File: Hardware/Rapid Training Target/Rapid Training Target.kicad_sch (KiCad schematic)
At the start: 15 parts, among them Q1 2N7002, Q2 2N7002, Q3 2N7002

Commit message: added code and remote
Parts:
- removed U1: ~, Personal:ESP32-C3-DevKit, symbol personal2:ESP32-C3_DevKit_Rev_A
- added C1, C2: 1u, Capacitor_SMD:C_0603_1608Metric, symbol Device:C
- added R1, R2: 5k1, Resistor_SMD:R_0603_1608Metric, symbol Device:R
- added U2: MIC5504-3.3YM5, Package_TO_SOT_SMD:SOT-23-5, symbol Regulator_Linear:MIC5504-3.3YM5
- added U3: ESP32-C3-MINI-1-N4, Personal:ESP32-­C3-­MINI­-1, symbol personal2:ESP32-­C3-­MINI­-1
- added USB-C1: USB-C-16P-F(A40-00119-A52-12), Personal:USB2.0_TYPE-C(A40-00119-A52-12), symbol personal2:USB2.0_TYPE-C(A40-00119-A52-12)
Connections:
- net +3V3: now also C1.1, U2.5 (VOUT), U3.3 (3V3), U3.8 (EN)
- net +5V: now also C2.1, U2.1 (VIN), U2.3 (EN), USB-C1.A4 (VBUS), USB-C1.A9 (VBUS), USB-C1.B4 (VBUS), USB-C1.B9 (VBUS)
- net Blue: now also U3.20 (IO6/GPIO6/FSPICLK/MTCK)
- net GND: now also C1.2, C2.2, R1.2, R2.2, U2.2 (GND), U3.1 (GND), U3.11 (GND), U3.14 (GND), U3.2 (GND), U3.36 (GND), U3.37 (GND), U3.38 (GND), U3.39 (GND), U3.40 (GND), U3.41 (GND), U3.42 (GND), U3.43 (GND), U3.44 (GND), U3.45 (GND), U3.46 (GND), U3.47 (GND), U3.48 (GND), U3.49 (GND), U3.50 (GND), U3.51 (GND), U3.52 (GND), U3.53 (GND), USB-C1.0 (SHELL), USB-C1.A1 (GND), USB-C1.A12 (GND), USB-C1.B1 (GND), USB-C1.B12 (GND)
- net Green: now also U3.19 (IO5/GPIO5/ADC2_CH0/FSPIWP/MTDI)
- net Red: now also U3.18 (IO4/GPIO4/ADC1_CH4/FSPIHD/MTMS)
- new net: R2.1, USB-C1.A5 (CC1)
- new net: R1.1, USB-C1.B5 (CC2)
- new net USB_D+: U3.27 (IO19/GPIO19/USB_D+), USB-C1.A6 (DP1), USB-C1.B6 (DP2)
- new net USB_D-: U3.26 (IO18/GPIO18/USB_D-), USB-C1.A7 (DN1), USB-C1.B7 (DN2)
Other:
- moved on the sheet: H1, H2, H3

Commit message: added logo
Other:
- note added: "Blue: 2.2V 1mA 25mcd 2.2k"
- note added: "Green: 2.3V 1mA 130mcd 120k"
- note added: "Red: 3.2V 1mA 45mcd 5.76k"
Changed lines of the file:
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@@
     (stroke (width 0) (type default))
+  )
+  (text "Green:\n2.3V\n1mA\n130mcd\n120k\n" (at 111.76 35.56 0)
+    (effects (font (size 1.27 1.27)) (justify left bottom))
+  )
+  (text "Blue:\n2.2V\n1mA\n25mcd\n2.2k\n" (at 119.38 35.56 0)
+    (effects (font (size 1.27 1.27)) (justify left bottom))
+  )
+  (text "Red:\n3.2V\n1mA\n45mcd\n5.76k\n" (at 104.14 35.56 0)
+    (effects (font (size 1.27 1.27)) (justify left bottom))
   )
   (global_label "Red" (shape input) (at 214.63 77.47 0) (fields_autoplaced)

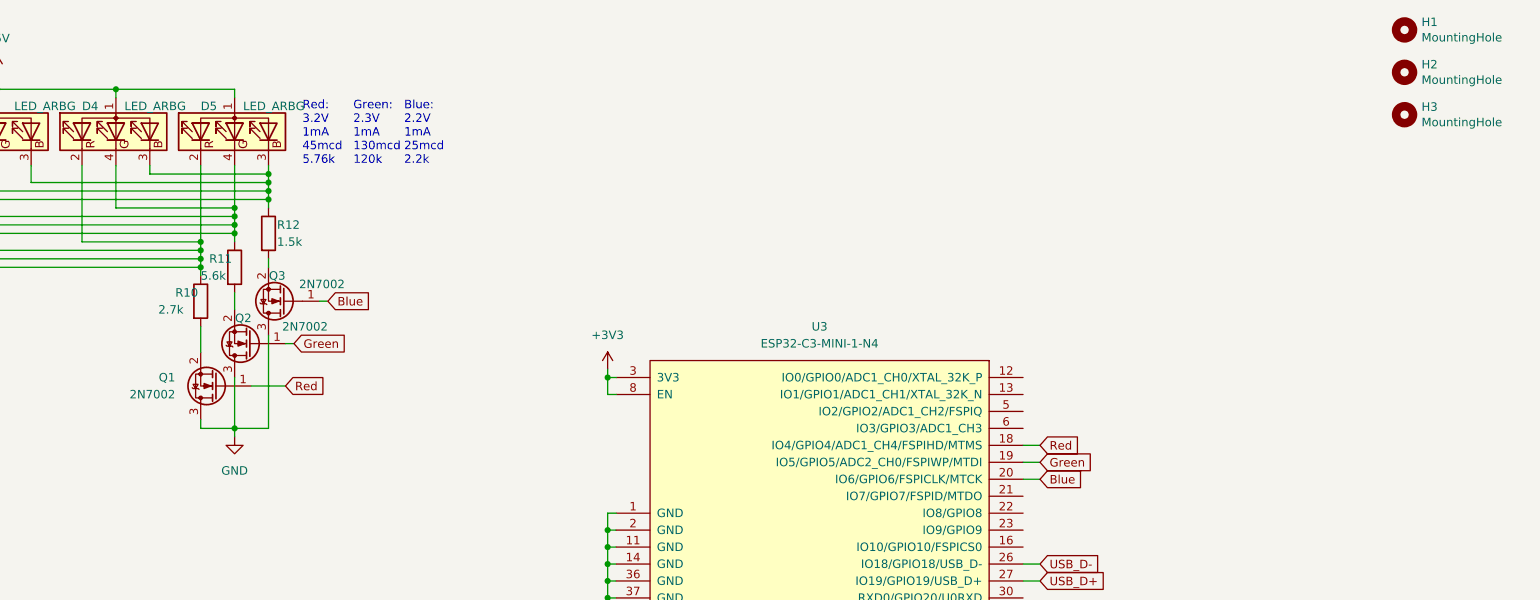
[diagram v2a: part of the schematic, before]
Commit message: rounded off edges and created a step
removed the use of mosfets for driving leds as found to be obsolete. Rounded corners, added a size indicator. changed the
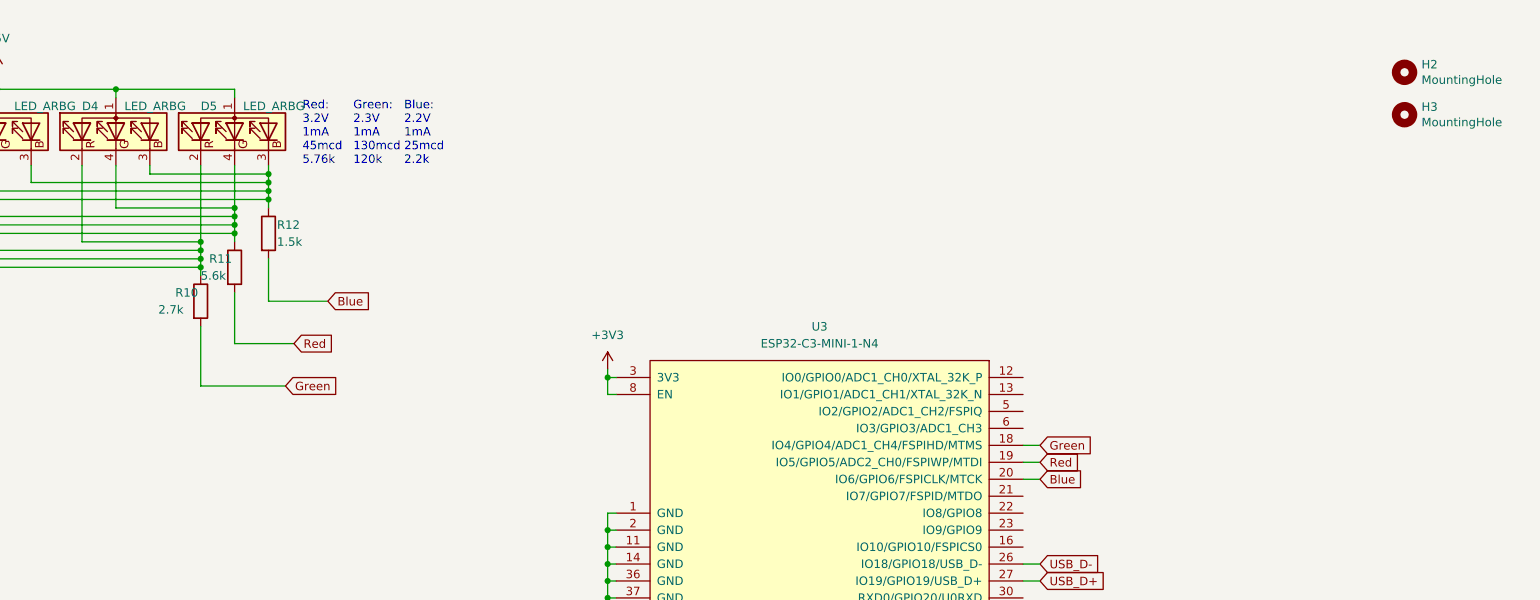
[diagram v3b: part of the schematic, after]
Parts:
- removed H1: MountingHole, MountingHole:MountingHole_3.2mm_M3_DIN965_Pad, symbol Mechanical:MountingHole
- removed Q1, Q2, Q3: 2N7002, Package_TO_SOT_SMD:SOT-23, symbol Transistor_FET:2N7002
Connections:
- net Blue: now also R12.2
- net Green: now also R10.2, U3.18 (IO4/GPIO4/ADC1_CH4/FSPIHD/MTMS); no longer U3.19 (IO5/GPIO5/ADC2_CH0/FSPIWP/MTDI)
- net Red: now also R11.2, U3.19 (IO5/GPIO5/ADC2_CH0/FSPIWP/MTDI); no longer U3.18 (IO4/GPIO4/ADC1_CH4/FSPIHD/MTMS)

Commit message: added initial cad
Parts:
- renumbered R11 to R1, R12 to R2, R10 to R3, R2 to R4, R1 to R5, U2 to U1, U3 to U2
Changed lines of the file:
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@@
   (symbol (lib_id "Device:R") (at 38.1 166.37 0) (mirror y) (unit 1)
     (in_bom yes) (on_board yes) (dnp no) (fields_autoplaced)
-    (property "Reference" "R2" (at 40.64 165.1 0)
+    (property "Reference" "R4" (at 40.64 165.1 0)
       (effects (font (size 1.27 1.27)) (justify right))
     )
@@
       (project "Rapid Training Target"
         (path "/9fedd953-8356-4168-99e6-03d50e1e6951"
-          (reference "R2") (unit 1)
+          (reference "R4") (unit 1)
         )
       )
@@
   (symbol (lib_id "Device:R") (at 88.9 55.88 0) (unit 1)
     (in_bom yes) (on_board yes) (dnp no)
-    (property "Reference" "R10" (at 85.09 54.61 0)
+    (property "Reference" "R3" (at 85.09 54.61 0)
       (effects (font (size 1.27 1.27)) (justify left))
     )
@@
       (project "Rapid Training Target"
         (path "/9fedd953-8356-4168-99e6-03d50e1e6951"
-          (reference "R10") (unit 1)
+          (reference "R3") (unit 1)
         )
       )
@@
   (symbol (lib_id "Device:R") (at 99.06 45.72 0) (unit 1)
     (in_bom yes) (on_board yes) (dnp no)
-    (property "Reference" "R12" (at 100.33 44.45 0)
+    (property "Reference" "R2" (at 100.33 44.45 0)
       (effects (font (size 1.27 1.27)) (justify left))
     )
@@
       (project "Rapid Training Target"
         (path "/9fedd953-8356-4168-99e6-03d50e1e6951"
-          (reference "R12") (unit 1)
+          (reference "R2") (unit 1)
         )
       )
@@
   (symbol (lib_id "personal2:ESP32-­C3-­MINI­-1") (at 207.01 64.77 0) (mirror y) (unit 1)
     (in_bom yes) (on_board yes) (dnp no)
-    (property "Reference" "U3" (at 181.61 59.69 0)
+    (property "Reference" "U2" (at 181.61 59.69 0)
       (effects (font (size 1.27 1.27)))
     )
@@
       (project "Rapid Training Target"
         (path "/9fedd953-8356-4168-99e6-03d50e1e6951"
-          (reference "U3") (unit 1)
+          (reference "U2") (unit 1)
         )
       )
@@
   (symbol (lib_id "Device:R") (at 35.56 166.37 0) (unit 1)
     (in_bom yes) (on_board yes) (dnp no)
-    (property "Reference" "R1" (at 33.02 165.1 0)
+    (property "Reference" "R5" (at 33.02 165.1 0)
       (effects (font (size 1.27 1.27)) (justify right))
     )
@@
       (project "Rapid Training Target"
         (path "/9fedd953-8356-4168-99e6-03d50e1e6951"
-          (reference "R1") (unit 1)
+          (reference "R5") (unit 1)
         )
       )
@@
   (symbol (lib_id "Regulator_Linear:MIC5504-3.3YM5") (at 34.29 104.14 0) (unit 1)
     (in_bom yes) (on_board yes) (dnp no) (fields_autoplaced)
-    (property "Reference" "U2" (at 34.29 93.98 0)
+    (property "Reference" "U1" (at 34.29 93.98 0)
       (effects (font (size 1.27 1.27)))
     )
@@
       (project "Rapid Training Target"
         (path "/9fedd953-8356-4168-99e6-03d50e1e6951"
-          (reference "U2") (unit 1)
+          (reference "U1") (unit 1)
         )
       )
@@
   (symbol (lib_id "Device:R") (at 93.98 50.8 0) (unit 1)
     (in_bom yes) (on_board yes) (dnp no)
-    (property "Reference" "R11" (at 90.17 49.53 0)
+    (property "Reference" "R1" (at 90.17 49.53 0)
       (effects (font (size 1.27 1.27)) (justify left))
     )
@@
       (project "Rapid Training Target"
         (path "/9fedd953-8356-4168-99e6-03d50e1e6951"
-          (reference "R11") (unit 1)
-        )
-      )
+          (reference "R1") (unit 1)
+        )
+      )

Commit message: changes to 3.3v
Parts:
- renumbered C2 to C1, C1 to C2, H2 to H1, H3 to H2, R4 to R1, R1 to R2, R2 to R3, R3 to R4
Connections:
- net +3V3: now also D1.1 (A), D2.1 (A), D3.1 (A), D4.1 (A), D5.1 (A)
- net +5V: no longer D1.1 (A), D2.1 (A), D3.1 (A), D4.1 (A), D5.1 (A)
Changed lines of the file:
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@@
-    )
-  )
-  (symbol (lib_id "power:+5V") (at 58.42 21.59 0) (unit 1)
-    (in_bom yes) (on_board yes) (dnp no) (fields_autoplaced)
-    (property "Reference" "#PWR03" (at 58.42 25.4 0)
-      (effects (font (size 1.27 1.27)) hide)
-    )
-    (property "Value" "+5V" (at 58.42 16.51 0)
-      (effects (font (size 1.27 1.27)))
-    )
-    (property "Footprint" "" (at 58.42 21.59 0)
-      (effects (font (size 1.27 1.27)) hide)
-    )
-    (property "Datasheet" "" (at 58.42 21.59 0)
-      (effects (font (size 1.27 1.27)) hide)
-    )
-    (pin "1")
-    (instances
-      (project "Rapid Training Target"
-        (path "/9fedd953-8356-4168-99e6-03d50e1e6951"
-          (reference "#PWR03") (unit 1)
-        )
-      )
-      (project "Training Aid-B"
-        (path "/e219089c-061e-4d60-9bdd-f96cb714b740"
-          (reference "#PWR0102") (unit 1)
-        )
-      )
     )
   )
@@
   (symbol (lib_id "Device:R") (at 38.1 166.37 0) (mirror y) (unit 1)
     (in_bom yes) (on_board yes) (dnp no) (fields_autoplaced)
-    (property "Reference" "R4" (at 40.64 165.1 0)
+    (property "Reference" "R1" (at 40.64 165.1 0)
       (effects (font (size 1.27 1.27)) (justify right))
     )
@@
       (project "Rapid Training Target"
         (path "/9fedd953-8356-4168-99e6-03d50e1e6951"
-          (reference "R4") (unit 1)
+          (reference "R1") (unit 1)
         )
       )
@@
   (symbol (lib_id "Device:C") (at 45.72 106.68 0) (unit 1)
     (in_bom yes) (on_board yes) (dnp no) (fields_autoplaced)
-    (property "Reference" "C1" (at 49.53 105.41 0)
+    (property "Reference" "C2" (at 49.53 105.41 0)
       (effects (font (size 1.27 1.27)) (justify left))
     )
@@
       (project "Rapid Training Target"
         (path "/9fedd953-8356-4168-99e6-03d50e1e6951"
-          (reference "C1") (unit 1)
+          (reference "C2") (unit 1)
         )
       )
@@
   (symbol (lib_id "Mechanical:MountingHole") (at 269.24 21.59 0) (unit 1)
     (in_bom yes) (on_board yes) (dnp no)
-    (property "Reference" "H2" (at 271.78 20.4216 0)
+    (property "Reference" "H1" (at 271.78 20.4216 0)
       (effects (font (size 1.27 1.27)) (justify left))
     )
@@
       (project "Rapid Training Target"
         (path "/9fedd953-8356-4168-99e6-03d50e1e6951"
+          (reference "H1") (unit 1)
+        )
+      )
+      (project "Training Aid-B"
+        (path "/e219089c-061e-4d60-9bdd-f96cb714b740"
           (reference "H2") (unit 1)
         )
       )
-      (project "Training Aid-B"
-        (path "/e219089c-061e-4d60-9bdd-f96cb714b740"
+    )
+  )
+  (symbol (lib_id "Mechanical:MountingHole") (at 269.24 27.94 0) (unit 1)
+    (in_bom yes) (on_board yes) (dnp no)
+    (property "Reference" "H2" (at 271.78 26.7716 0)
+      (effects (font (size 1.27 1.27)) (justify left))
+    )
+    (property "Value" "MountingHole" (at 271.78 29.083 0)
+      (effects (font (size 1.27 1.27)) (justify left))
+    )
+    (property "Footprint" "MountingHole:MountingHole_3.2mm_M3_DIN965_Pad" (at 269.24 27.94 0)
+      (effects (font (size 1.27 1.27)) hide)
+    )
+    (property "Datasheet" "~" (at 269.24 27.94 0)
+      (effects (font (size 1.27 1.27)) hide)
+    )
+    (instances
+      (project "Rapid Training Target"
+        (path "/9fedd953-8356-4168-99e6-03d50e1e6951"
           (reference "H2") (unit 1)
-        )
-      )
-    )
-  )
-  (symbol (lib_id "Mechanical:MountingHole") (at 269.24 27.94 0) (unit 1)
-    (in_bom yes) (on_board yes) (dnp no)
-    (property "Reference" "H3" (at 271.78 26.7716 0)
-      (effects (font (size 1.27 1.27)) (justify left))
-    )
-    (property "Value" "MountingHole" (at 271.78 29.083 0)
-      (effects (font (size 1.27 1.27)) (justify left))
-    )
-    (property "Footprint" "MountingHole:MountingHole_3.2mm_M3_DIN965_Pad" (at 269.24 27.94 0)
-      (effects (font (size 1.27 1.27)) hide)
-    )
-    (property "Datasheet" "~" (at 269.24 27.94 0)
-      (effects (font (size 1.27 1.27)) hide)
-    )
-    (instances
-      (project "Rapid Training Target"
-        (path "/9fedd953-8356-4168-99e6-03d50e1e6951"
-          (reference "H3") (unit 1)
         )
       )
@@
     )
   )
+  (symbol (lib_id "power:+3V3") (at 58.42 21.59 0) (unit 1)
+    (in_bom yes) (on_board yes) (dnp no) (fields_autoplaced)
+    (property "Reference" "#PWR02" (at 58.42 25.4 0)
+      (effects (font (size 1.27 1.27)) hide)
+    )
+    (property "Value" "+3V3" (at 58.42 16.51 0)
+      (effects (font (size 1.27 1.27)))
+    )
+    (property "Footprint" "" (at 58.42 21.59 0)
+      (effects (font (size 1.27 1.27)) hide)
+    )
+    (property "Datasheet" "" (at 58.42 21.59 0)
+      (effects (font (size 1.27 1.27)) hide)
+    )
+    (pin "1")
+    (instances
+      (project "Rapid Training Target"
+        (path "/9fedd953-8356-4168-99e6-03d50e1e6951"
+          (reference "#PWR02") (unit 1)
+        )
+      )
+    )
+  )
   (symbol (lib_name "+5V_2") (lib_id "power:+5V") (at 30.48 129.54 0) (unit 1)
     (in_bom yes) (on_board yes) (dnp no) (fields_autoplaced)
@@
   (symbol (lib_id "Device:R") (at 88.9 55.88 0) (unit 1)
     (in_bom yes) (on_board yes) (dnp no)
-    (property "Reference" "R3" (at 85.09 54.61 0)
+    (property "Reference" "R4" (at 85.09 54.61 0)
       (effects (font (size 1.27 1.27)) (justify left))
     )
@@
       (project "Rapid Training Target"
         (path "/9fedd953-8356-4168-99e6-03d50e1e6951"
-          (reference "R3") (unit 1)
+          (reference "R4") (unit 1)
         )
       )
@@
   (symbol (lib_id "Device:R") (at 99.06 45.72 0) (unit 1)
     (in_bom yes) (on_board yes) (dnp no)
-    (property "Reference" "R2" (at 100.33 44.45 0)
+    (property "Reference" "R3" (at 100.33 44.45 0)
       (effects (font (size 1.27 1.27)) (justify left))
     )
@@
       (project "Rapid Training Target"
         (path "/9fedd953-8356-4168-99e6-03d50e1e6951"
-          (reference "R2") (unit 1)
+          (reference "R3") (unit 1)
         )
       )
@@
   (symbol (lib_id "Device:C") (at 21.59 106.68 0) (mirror y) (unit 1)
     (in_bom yes) (on_board yes) (dnp no)
-    (property "Reference" "C2" (at 17.78 105.41 0)
+    (property "Reference" "C1" (at 17.78 105.41 0)
       (effects (font (size 1.27 1.27)) (justify left))
     )
@@
       (project "Rapid Training Target"
         (path "/9fedd953-8356-4168-99e6-03d50e1e6951"
-          (reference "C2") (unit 1)
+          (reference "C1") (unit 1)
         )
       )
@@
   (symbol (lib_id "Device:R") (at 93.98 50.8 0) (unit 1)
     (in_bom yes) (on_board yes) (dnp no)
-    (property "Reference" "R1" (at 90.17 49.53 0)
+    (property "Reference" "R2" (at 90.17 49.53 0)
       (effects (font (size 1.27 1.27)) (justify left))
     )
@@
       (project "Rapid Training Target"
         (path "/9fedd953-8356-4168-99e6-03d50e1e6951"
-          (reference "R1") (unit 1)
-        )
-      )
+          (reference "R2") (unit 1)
+        )
+      )

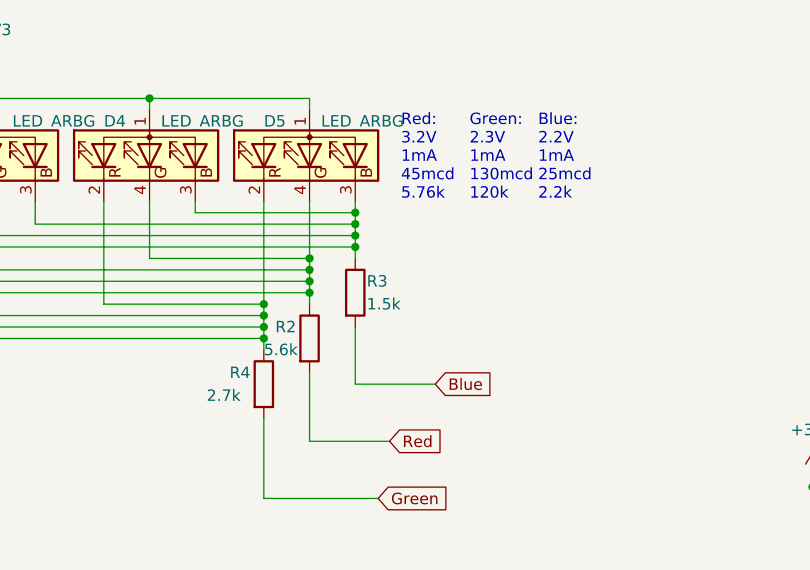
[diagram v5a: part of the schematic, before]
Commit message: changed to 0603 capacitors
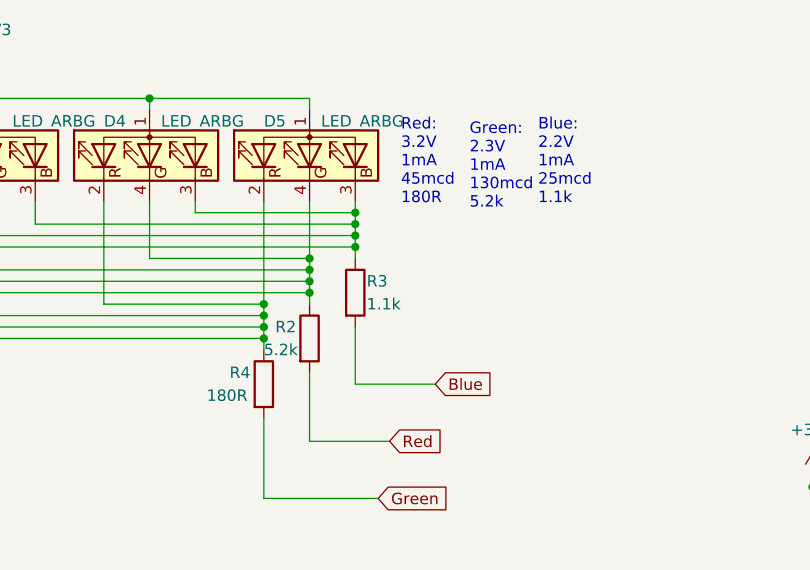
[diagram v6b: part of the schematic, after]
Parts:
- R2: value 5.6k -> 5.2k
- R3: value 1.5k -> 1.1k
- R4: value 2.7k -> 180R
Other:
- note added: "Blue: 2.2V 1mA 25mcd 1.1k"
- note added: "Green: 2.3V 1mA 130mcd 5.2k"
- note added: "Red: 3.2V 1mA 45mcd 180R"
- note removed: "Blue: 2.2V 1mA 25mcd 2.2k"
- note removed: "Green: 2.3V 1mA 130mcd 120k"
- note removed: "Red: 3.2V 1mA 45mcd 5.76k"
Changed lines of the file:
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@@
     (stroke (width 0) (type default))
   )
-  (text "Green:\n2.3V\n1mA\n130mcd\n120k\n" (at 111.76 35.56 0)
+  (text "Green:\n2.3V\n1mA\n130mcd\n5.2k\n\n\n" (at 111.76 40.64 0)
     (effects (font (size 1.27 1.27)) (justify left bottom))
   )
-  (text "Blue:\n2.2V\n1mA\n25mcd\n2.2k\n" (at 119.38 35.56 0)
+  (text "Blue:\n2.2V\n1mA\n25mcd\n1.1k\n\n" (at 119.38 38.1 0)
     (effects (font (size 1.27 1.27)) (justify left bottom))
   )
-  (text "Red:\n3.2V\n1mA\n45mcd\n5.76k\n" (at 104.14 35.56 0)
+  (text "Red:\n3.2V\n1mA\n45mcd\n180R\n\n" (at 104.14 38.1 0)
     (effects (font (size 1.27 1.27)) (justify left bottom))
   )
@@
       (effects (font (size 1.27 1.27)) (justify left))
     )
-    (property "Value" "2.7k" (at 82.55 57.15 0)
+    (property "Value" "180R" (at 82.55 57.15 0)
       (effects (font (size 1.27 1.27)) (justify left))
     )
@@
       (effects (font (size 1.27 1.27)) (justify left))
     )
-    (property "Value" "1.5k" (at 100.33 46.99 0)
+    (property "Value" "1.1k" (at 100.33 46.99 0)
       (effects (font (size 1.27 1.27)) (justify left))
     )
@@
       (effects (font (size 1.27 1.27)) (justify left))
     )
-    (property "Value" "5.6k" (at 88.9 52.07 0)
-      (effects (font (size 1.27 1.27)) (justify left))
-    )
+    (property "Value" "5.2k" (at 88.9 52.07 0)
+      (effects (font (size 1.27 1.27)) (justify left))
+    )
